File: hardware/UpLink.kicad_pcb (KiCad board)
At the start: 2 copper layers, 50 x 50 mm, 20 parts, among them U1 SAM-M10Q-00B, U2 XIAO-ESP32-S3-SMD, U3 114993390, U4 TPS631000DRLR

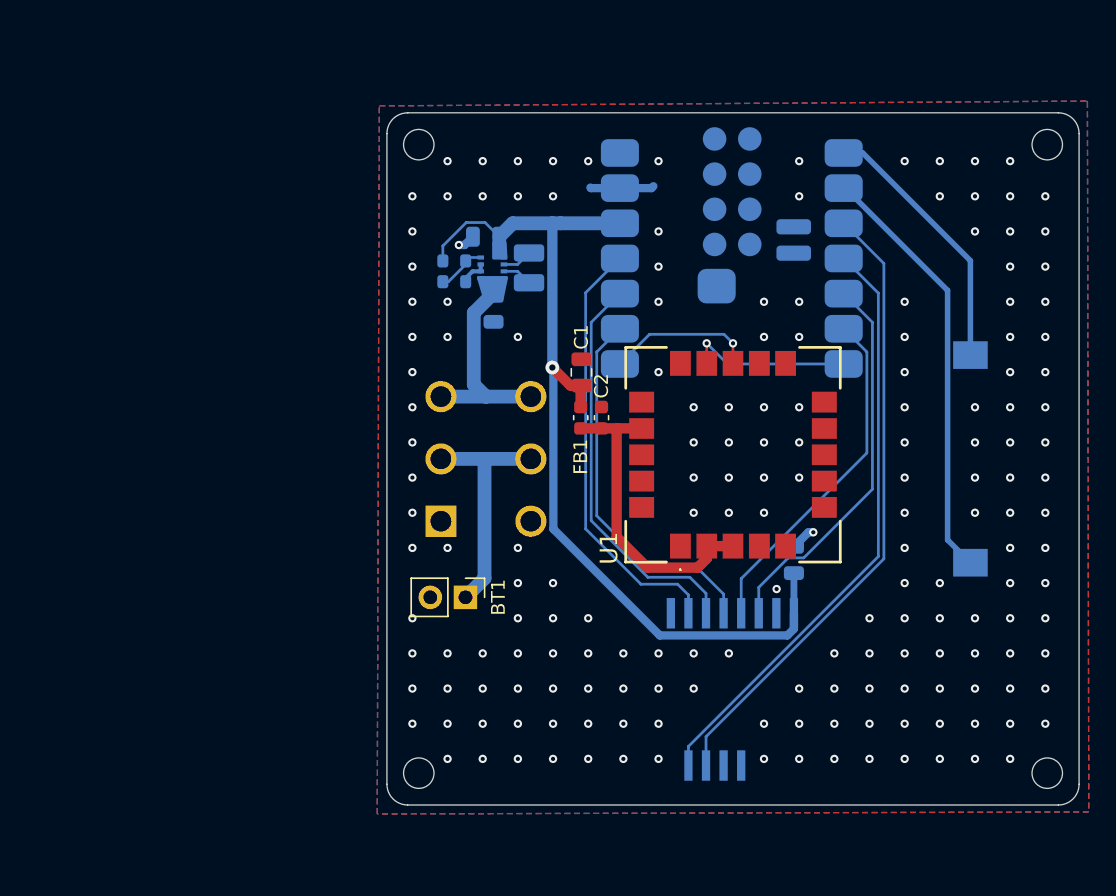
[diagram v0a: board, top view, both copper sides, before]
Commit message: Add TPS22917DBV for high side switching of payload, redesign layout for thinner board at cost of slight GPS performance hits
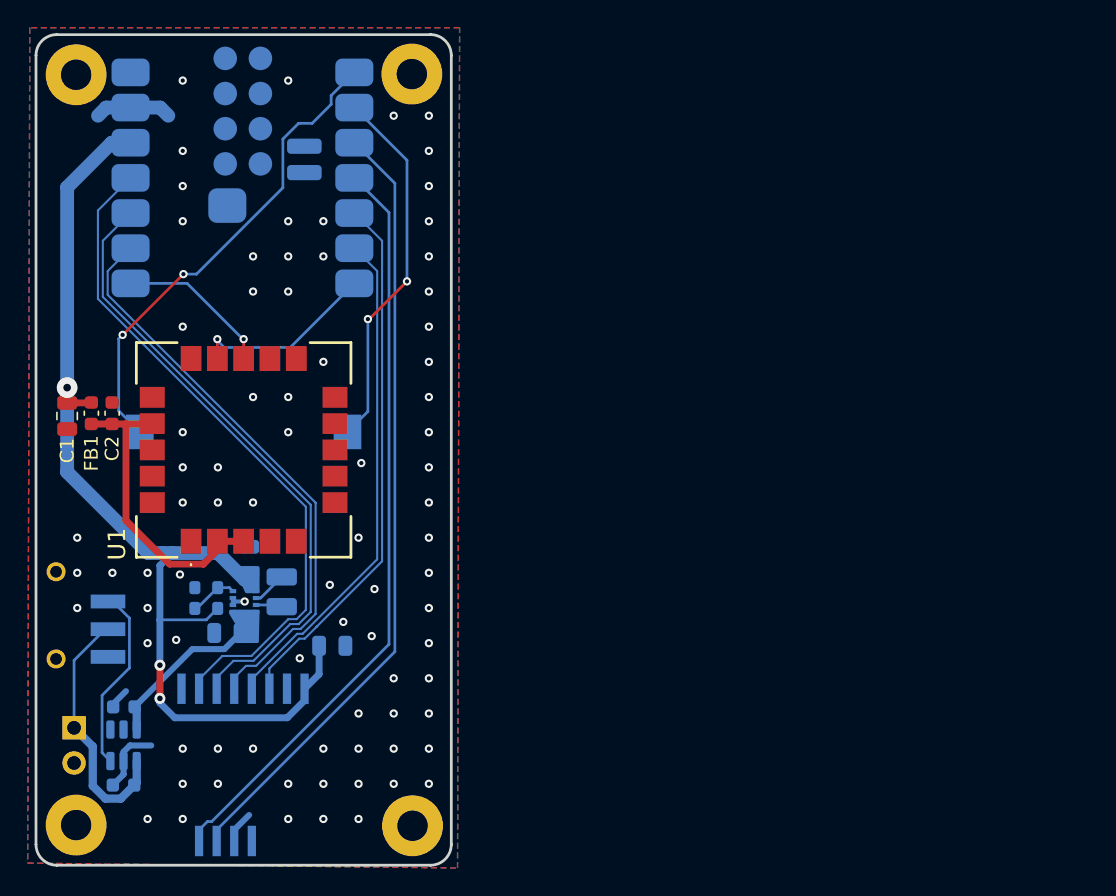
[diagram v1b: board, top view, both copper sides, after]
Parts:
- added C6: 1uF, Capacitor_SMD:C_0603_1608Metric, B.Cu at (103.6, 107.9)
- added C7: 100nF, Capacitor_SMD:C_0603_1608Metric, B.Cu at (103.7, 102.2)
- added U5: TPS22917DBV, Package_TO_SOT_SMD:SOT-23-6, B.Cu at (103.6, 105.0)
- BT1: moved to B.Cu
- H1, H2, H3, H4: footprint MountingHole:MountingHole_2.2mm_M2 -> MountingHole:MountingHole_2.2mm_M2_Pad
- S1: value SLW-1678105-6A-N-D -> CSS-1210TB; footprint SLW-1678105-6A-N-D:SLW16781056AND -> CSS-1210TB:CSS1210TB
- moved LS1 52.5 mm to (112.3, 82.3), turned to -90 degrees
- moved H2 46.2 mm to (124.5, 56.5)
- moved H4 46.0 mm to (124.5, 110.8)
- moved C1 37.3 mm to (99.5, 81.2), turned to -90 degrees
- moved U2 35.8 mm to (121.1, 74.5)
- moved U3 35.8 mm to (112.3, 106.4)
- moved U1 35.4 mm to (112.3, 83.7)
- moved C2 35.4 mm to (102.8, 81.0)
- moved FB1 35.4 mm to (101.3, 81.0)
- moved C3 33.9 mm to (118.7, 97.8), turned to 0 degrees
- moved R1 30.8 mm to (109.6, 95.1), turned to 180 degrees
- moved C4 30.3 mm to (111.1, 96.9), turned to 180 degrees
- moved U4 30.0 mm to (112.4, 94.6)
- moved BT1 29.8 mm to (100.0, 103.7), turned to 180 degrees
- moved L1 29.4 mm to (115.0, 93.9)
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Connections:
- S1 pad 3: +BATT -> Net-(U5-ON)
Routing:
- net LORA-MISO: track 31.3 -> 48.9 mm
- net LORA-MOSI: track 29.2 -> 45.4 mm
- net Net-(LS1-+): track 19.2 -> 34.8 mm, vias 0 -> 2
- net LORA-SCK: track 27.1 -> 41.9 mm
- net Net-(U5-ON): track 0.00 -> 13.4 mm
- net LORA-NRST: track 25.0 -> 36.5 mm
- net LORA-DIO1: track 43.4 -> 54.8 mm
- net LORA-BUSY: track 45.7 -> 57.0 mm
- net LORA-NSS: track 28.0 -> 38.9 mm
- net +3.3V: track 66.5 -> 77.2 mm, vias 1 -> 3
- net GND: track 9.77 -> 15.7 mm, vias 177 -> 81
- net Net-(LS1--): track 30.9 -> 26.8 mm, vias 0 -> 2
- net +BATT: track 16.5 -> 13.2 mm
- net GPS-RX: track 12.0 -> 13.5 mm
- net Net-(BT1-+): track 17.1 -> 18.6 mm
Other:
- board size 50 x 50 mm -> 30 x 60 mm

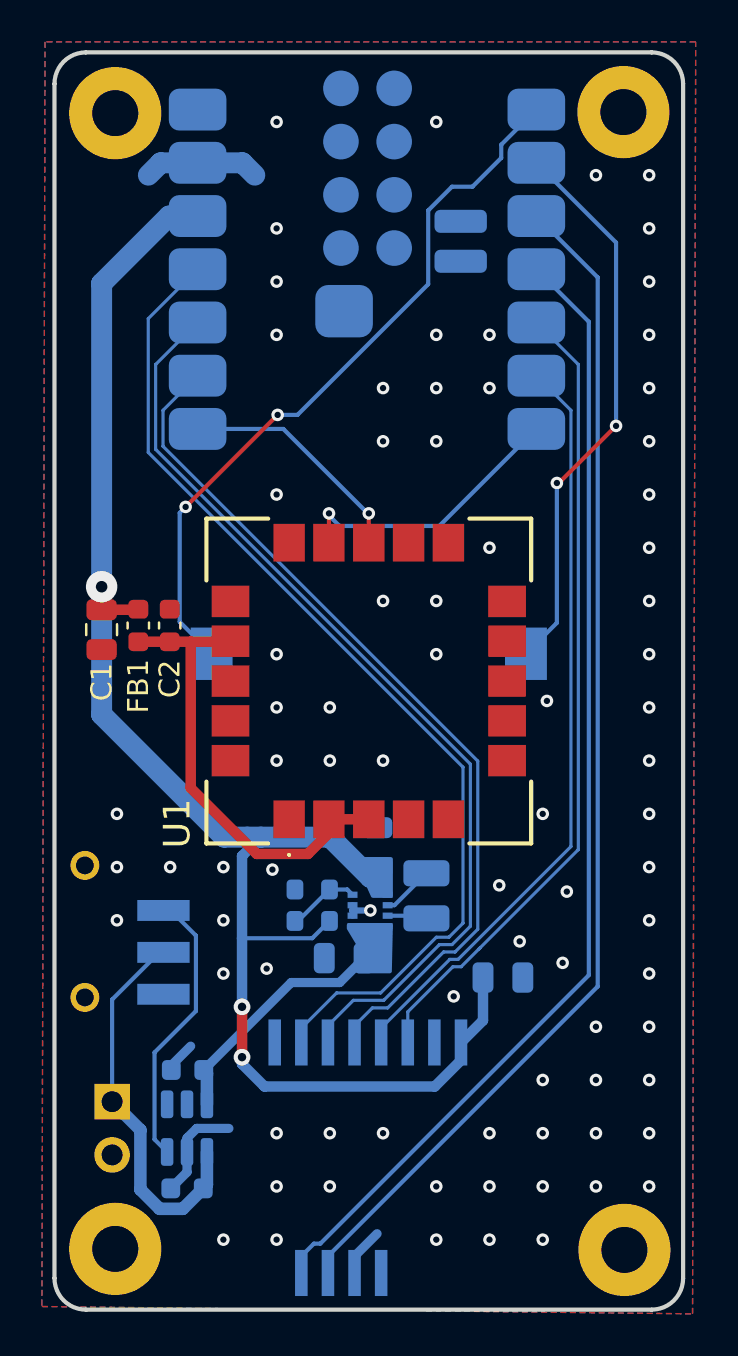
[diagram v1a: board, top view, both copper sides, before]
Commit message: Redo layout and routing, space traces apart
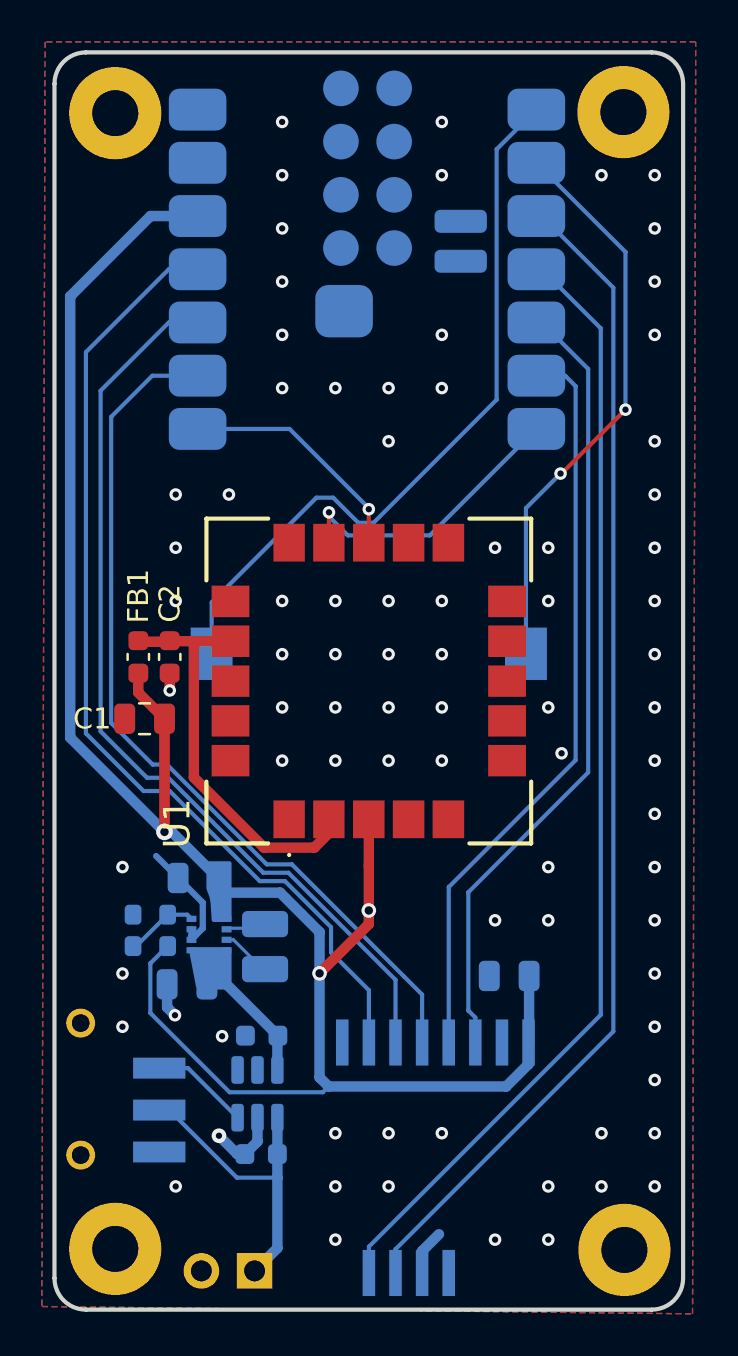
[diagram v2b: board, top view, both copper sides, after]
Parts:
- moved BT1 10.6 mm to (106.8, 111.8), turned to 90 degrees
- moved C5 8.67 mm to (104.2, 93.0), turned to 180 degrees
- moved L1 8.07 mm to (107.3, 96.3)
- moved R1 7.82 mm to (101.9, 96.3)
- moved R2 7.82 mm to (101.9, 94.8)
- moved U4 7.77 mm to (104.7, 95.8)
- moved C4 7.60 mm to (103.6, 98.1)
- moved S1 7.53 mm to (99.2, 103.1)
- moved C1 4.72 mm to (101.6, 85.5), turned to 180 degrees
- moved C6 3.90 mm to (107.2, 106.2)
- moved C7 3.90 mm to (107.2, 100.6)
- moved U5 3.74 mm to (107.0, 103.3)
- moved U3 3.23 mm to (115.5, 106.4)
- moved C2 1.50 mm to (102.8, 82.5), turned to -90 degrees
- moved FB1 1.50 mm to (101.3, 82.5), turned to 90 degrees
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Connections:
- U1 pad 3: Net-(U1-VCC) -> +3.3V
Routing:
- net +3.3V: track 77.2 -> 96.0 mm
- net Net-(U5-ON): track 13.4 -> 4.72 mm
- net +BATT: track 13.2 -> 6.05 mm
- net Net-(BT1-+): track 18.6 -> 14.7 mm
- net Net-(U1-VCC): track 22.3 -> 19.7 mm
- net LORA-MISO: track 48.9 -> 46.9 mm
- net GND: track 15.7 -> 13.8 mm, vias 81 -> 80
- net LORA-MOSI: track 45.4 -> 44.2 mm
- net Net-(LS1-+): track 34.8 -> 35.7 mm, vias 2 -> 0
- net LORA-DIO1: track 54.8 -> 53.9 mm
- net LORA-NSS: track 38.9 -> 38.0 mm
- net Net-(U4-LX2): track 2.48 -> 1.87 mm
- net LORA-NRST: track 36.5 -> 35.9 mm
- net LORA-BUSY: track 57.0 -> 56.4 mm
- net Net-(U4-LX1): track 1.90 -> 2.42 mm
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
